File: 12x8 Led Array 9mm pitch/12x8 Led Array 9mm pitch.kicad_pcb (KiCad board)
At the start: 4 copper layers, 173.7 x 137.7 mm, 313 parts, among them J1 LED ch 1-24, J2 LED ch 25-48, J3 LED ch 49-72, J4 LED ch 73-96, J5 logic/analog, U1 CD74HC4067M96, U2 CD74HC4067M96, U3 CD74HC4067M96, U4 CD74HC4067M96, U5 CD74HC4067M96, U6 CD74HC4067M96

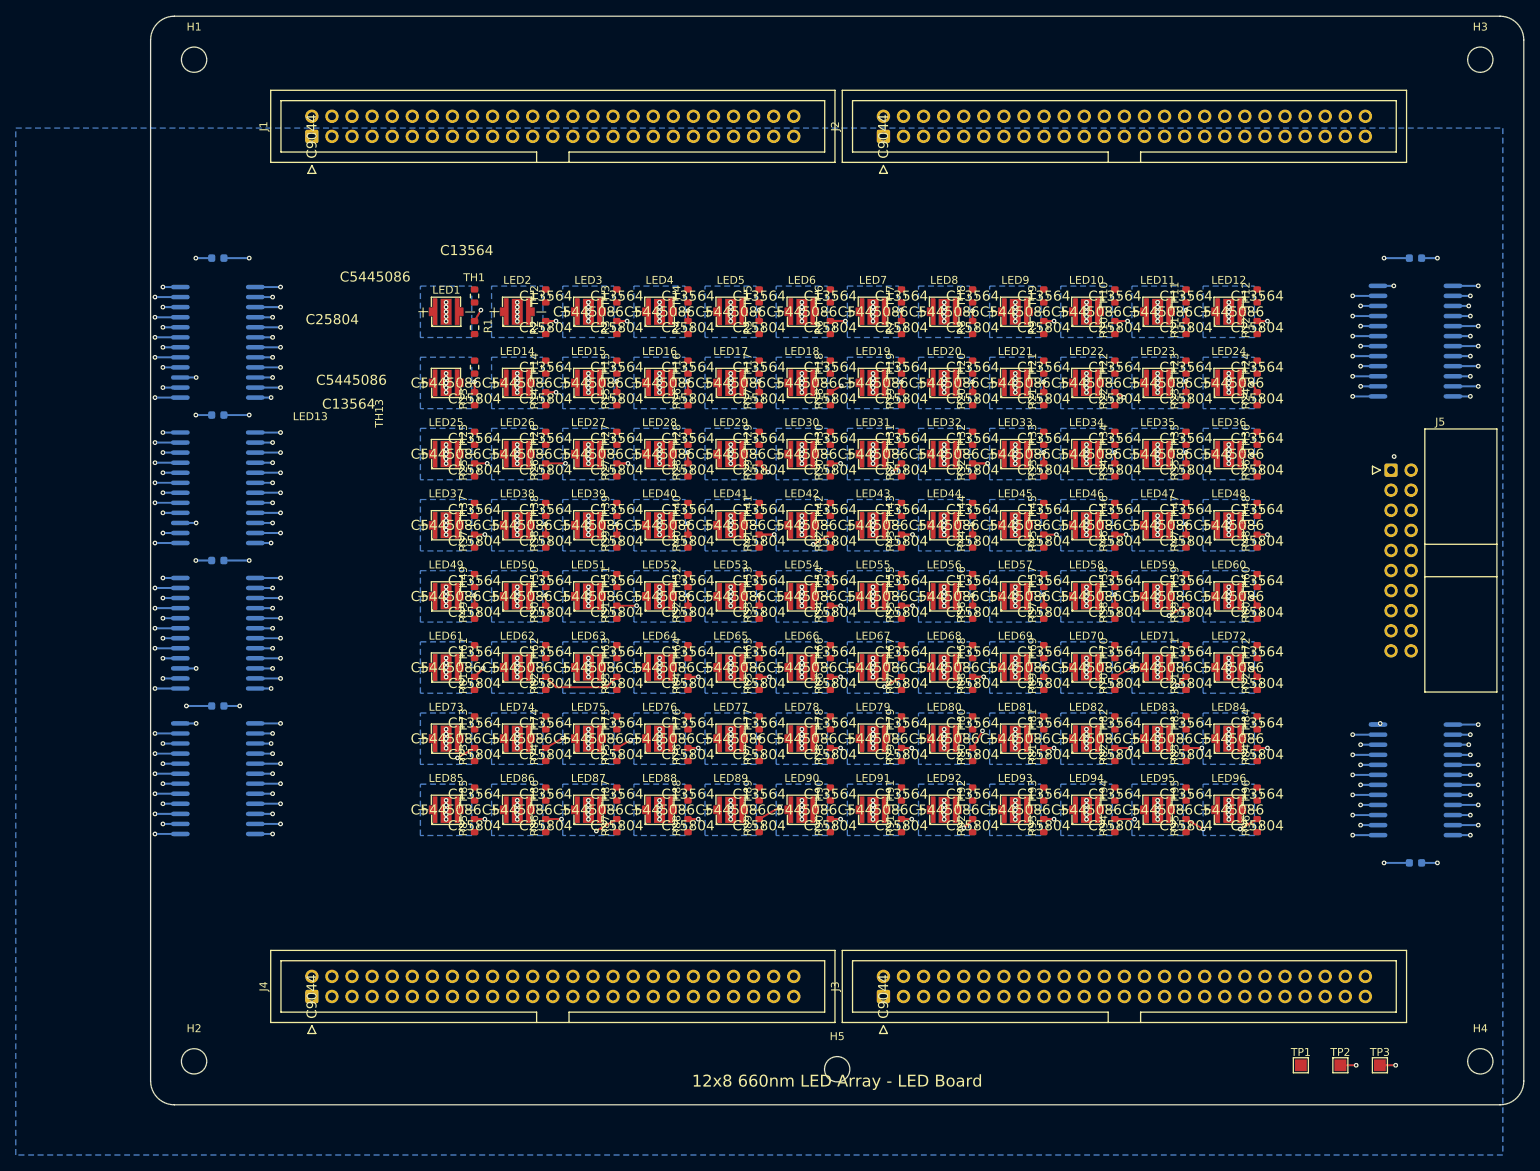
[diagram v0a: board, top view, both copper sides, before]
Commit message: Muxes and caps back to front side (single-sided assembly restored)
The back-side move no longer bought any board size (15mm keep-out +
J5 column set the width) while costing double-sided assembly and
unroutable pads. Fanout removed, parts unflipped in place, GND
re-stitched on front, placement DRC clean.

Co-Authored-By: Claude Fable 5 <noreply@anthropic.com>
Claude-Session: https://claude.ai/code/session_017oD54uh7Tvu54u9NPQNcZB
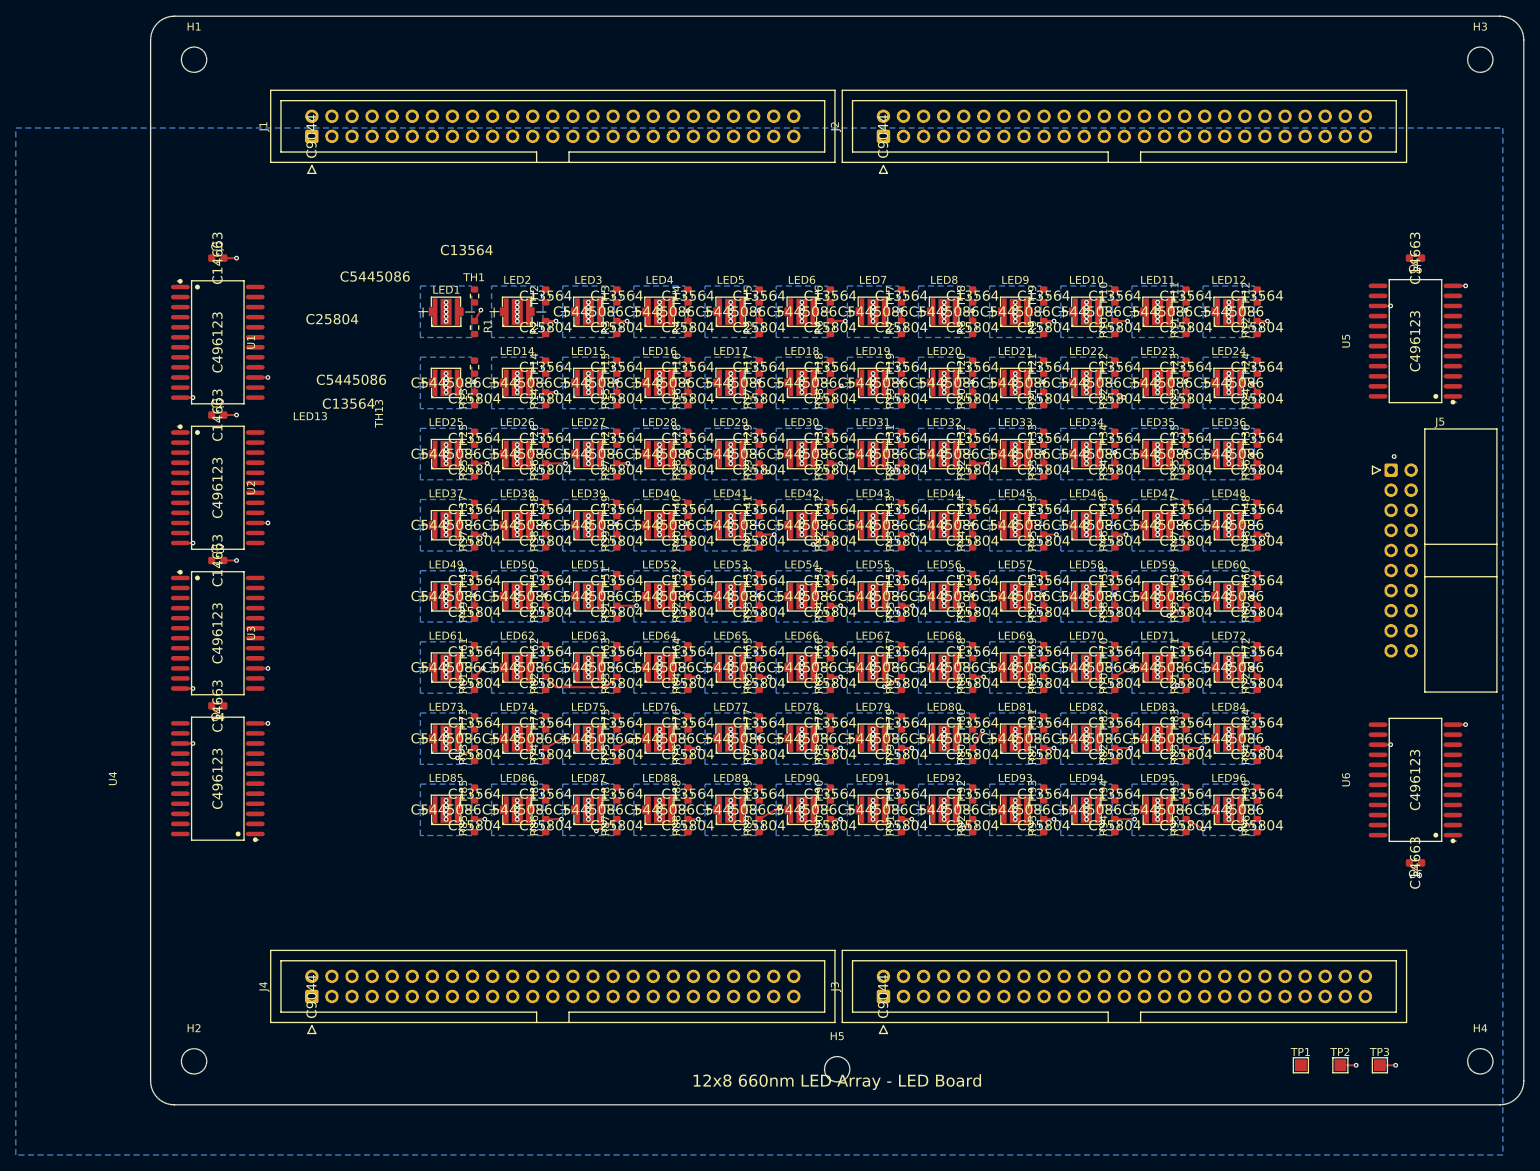
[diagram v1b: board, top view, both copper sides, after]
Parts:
- C1, C2, C3, C4, C5, C6, U1, U2, U3, U4, U5, U6: moved to F.Cu
- turned C1 to 0 degrees
- turned C2 to 0 degrees
- turned C3 to 0 degrees
- turned C4 to 180 degrees
- turned C5 to 180 degrees
- turned C6 to 180 degrees
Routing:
- net +3.3V: track 32.4 -> 0.00 mm, vias 12 -> 0
- net /MUX_A3: track 19.2 -> 0.00 mm, vias 6 -> 0
- net /MUX_A1: track 19.2 -> 0.00 mm, vias 6 -> 0
- net /MUX_A2: track 13.2 -> 0.00 mm, vias 6 -> 0
- net /MUX_A0: track 13.2 -> 0.00 mm, vias 6 -> 0
- net GND: track 198.7 -> 192.2 mm
- net /NTC_SIG4: track 3.20 -> 0.00 mm, vias 1 -> 0
- net /NTC_SIG3: track 3.20 -> 0.00 mm, vias 1 -> 0
- net /NTC_SIG2: track 3.20 -> 0.00 mm, vias 1 -> 0
- net /NTC_SIG1: track 3.20 -> 0.00 mm, vias 1 -> 0
- net /NTC92: track 3.20 -> 0.00 mm, vias 1 -> 0
- net /NTC90: track 3.20 -> 0.00 mm, vias 1 -> 0
- net /NTC88: track 3.20 -> 0.00 mm, vias 1 -> 0
- net /NTC86: track 3.20 -> 0.00 mm, vias 1 -> 0
- net /NTC79: track 3.20 -> 0.00 mm, vias 1 -> 0
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
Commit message: LED board routed: 4600+ tracks via Freerouting after back-side fix
97% complete - 15 connections left for manual routing (11 LED_K +
LED_A83 near J2/J4 outer pin rows, 3 GND edge pins). Dangling scraps
swept; zones filled.

Co-Authored-By: Claude Fable 5 <noreply@anthropic.com>
Claude-Session: https://claude.ai/code/session_017oD54uh7Tvu54u9NPQNcZB
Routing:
- net +3.3V: track 0.00 -> 2277.7 mm, vias 0 -> 11
- net /MUX_A1: track 0.00 -> 516.2 mm, vias 0 -> 7
- net /MUX_A3: track 0.00 -> 515.4 mm, vias 0 -> 6
- net /MUX_A2: track 0.00 -> 510.2 mm, vias 0 -> 6
- net /MUX_A0: track 0.00 -> 507.6 mm, vias 0 -> 6
- net /NTC86: track 0.00 -> 391.6 mm, vias 0 -> 2
- net /NTC20: track 0.00 -> 375.3 mm, vias 0 -> 2
- net /NTC_SIG4: track 0.00 -> 374.5 mm, vias 0 -> 2
- net /NTC19: track 0.00 -> 371.2 mm, vias 0 -> 4
- net /NTC_SIG1: track 0.00 -> 366.1 mm, vias 0 -> 1
- net /NTC_SIG2: track 0.00 -> 350.8 mm, vias 0 -> 2
- net /NTC_SIG3: track 0.00 -> 300.2 mm, vias 0 -> 4
- net /NTC56: track 0.00 -> 297.1 mm, vias 0 -> 4
- net /NTC7: track 0.00 -> 295.6 mm, vias 0 -> 4
- net /NTC31: track 0.00 -> 294.2 mm, vias 0 -> 4
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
